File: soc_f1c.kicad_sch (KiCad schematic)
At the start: 30 parts, among them U3 F1C100S, Y1 24Mhz 12pF

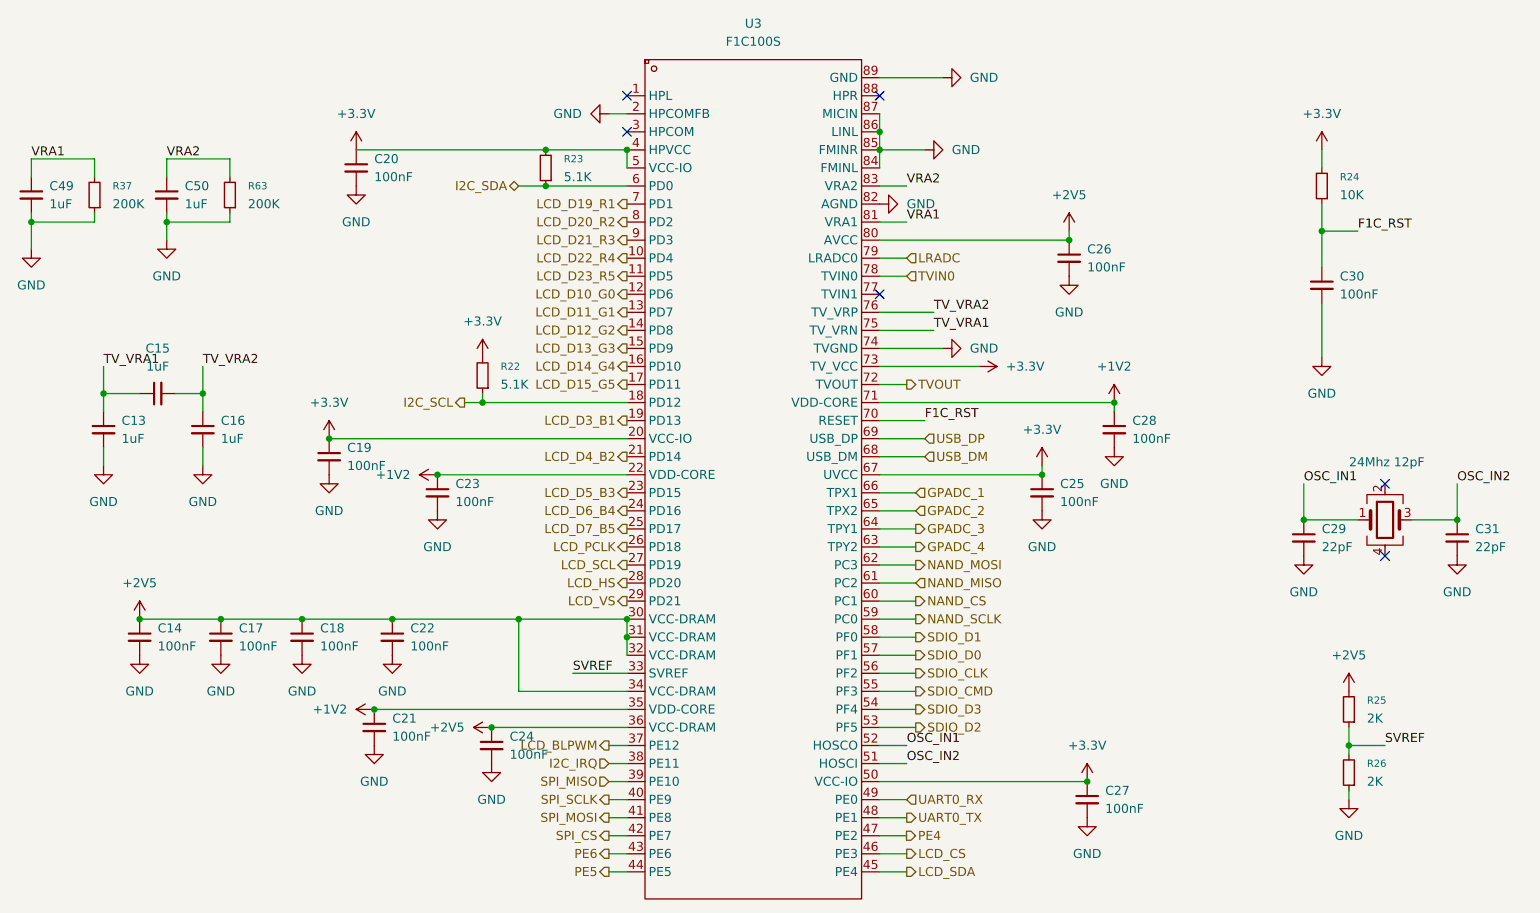
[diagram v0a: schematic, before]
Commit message: V0.3.1 bugfix
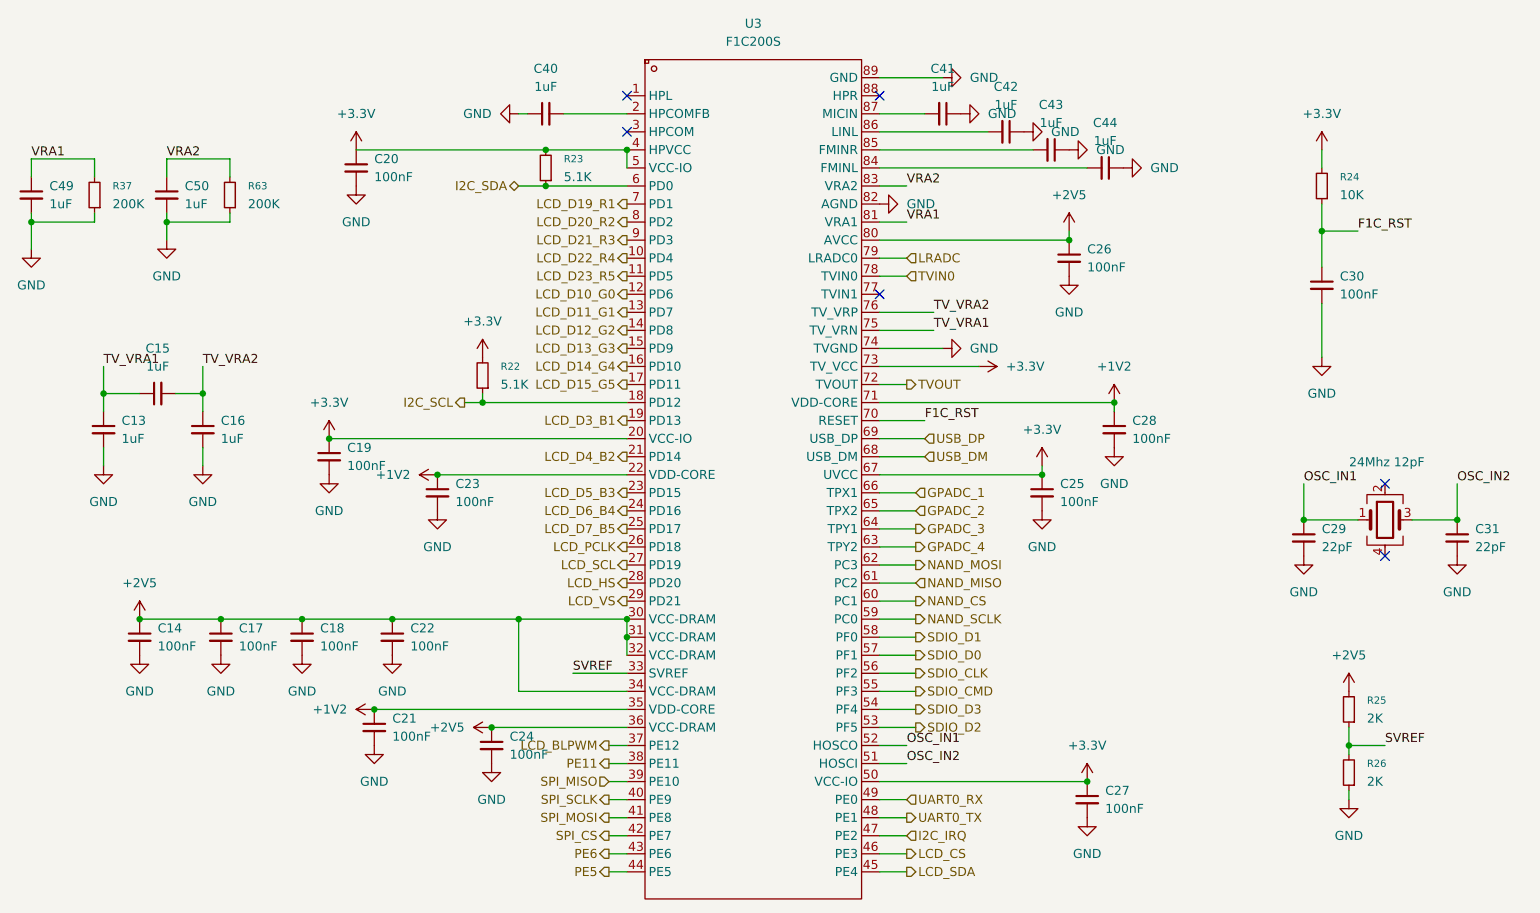
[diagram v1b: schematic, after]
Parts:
- added C40, C41, C42, C43, C44: 1uF, Capacitor_SMD:C_0603_1608Metric, symbol Device:C_Small
- U3: value F1C100S -> F1C200S; 特殊说明 (none) -> 不要购买”新版本“！
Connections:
- net PE4 is gone; now on net I2C_IRQ: U3.47 (PE2)
- net GND: now also C40.1, C41.1, C42.1, C43.1, C44.1; no longer U3.2 (HPCOMFB), U3.84 (FMINL), U3.85 (FMINR), U3.86 (LINL), U3.87 (MICIN)
- net I2C_IRQ: no longer U3.38 (PE11)
- new net: C43.2, U3.85 (FMINR)
- new net: C40.2, U3.2 (HPCOMFB)
- new net: C42.2, U3.86 (LINL)
- new net: C44.2, U3.84 (FMINL)
- new net: C41.2, U3.87 (MICIN)
- new net PE11: U3.38 (PE11)

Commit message: V0.5
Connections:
- net PE11 is gone; now on net LCD_CS: U3.38 (PE11)
- net LCD_CS: no longer U3.46 (PE3)
- net I2C_IRQ renamed PWR_SHUTDOWN
- new net PE3: U3.46 (PE3)
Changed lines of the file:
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@@
 		(comment 1 "V0.3 添加屏幕兼容接口，添加SD卡槽，优化布线")
 		(comment 2 "V0.3.1 BUG修复")
+		(comment 3 "土豆、星语Studio、爱莉希雅、所有复刻群友的支持！")
+		(comment 4 "V0.3.2 生产优化。特别感谢：（不分先后）和光、薄云、烟雨、WXNA、")
 	)
 	(junction
@@
 		)
 	)
-	(hierarchical_label "I2C_IRQ"
-		(shape input)
+	(hierarchical_label "PWR_SHUTDOWN"
+		(shape output)
 		(at 167.64 151.13 0)
 		(effects
@@
 		)
 	)
+	(hierarchical_label "LCD_CS"
+		(shape output)
+		(at 125.73 140.97 180)
+		(effects
+			(font
+				(size 1.27 1.27)
+			)
+			(justify right)
+		)
+	)
 	(hierarchical_label "LCD_D6_B4"
 		(shape output)
@@
 		)
 	)
-	(hierarchical_label "PE11"
-		(shape output)
-		(at 125.73 140.97 180)
-		(effects
-			(font
-				(size 1.27 1.27)
-			)
-			(justify right)
-		)
-	)
 	(hierarchical_label "SDIO_D1"
 		(shape output)
@@
 		)
 	)
-	(hierarchical_label "LCD_CS"
+	(hierarchical_label "SPI_CS"
+		(shape output)
+		(at 125.73 151.13 180)
+		(effects
+			(font
+				(size 1.27 1.27)
+			)
+			(justify right)
+		)
+	)
+	(hierarchical_label "LCD_SCL"
+		(shape output)
+		(at 128.27 113.03 180)
+		(effects
+			(font
+				(size 1.27 1.27)
+			)
+			(justify right)
+		)
+	)
+	(hierarchical_label "I2C_SCL"
+		(shape output)
+		(at 105.41 90.17 180)
+		(effects
+			(font
+				(size 1.27 1.27)
+			)
+			(justify right)
+		)
+	)
+	(hierarchical_label "SDIO_D2"
+		(shape output)
+		(at 168.91 135.89 0)
+		(effects
+			(font
+				(size 1.27 1.27)
+			)
+			(justify left)
+		)
+	)
+	(hierarchical_label "SDIO_CLK"
+		(shape output)
+		(at 168.91 128.27 0)
+		(effects
+			(font
+				(size 1.27 1.27)
+			)
+			(justify left)
+		)
+	)
+	(hierarchical_label "SPI_MOSI"
+		(shape output)
+		(at 125.73 148.59 180)
+		(effects
+			(font
+				(size 1.27 1.27)
+			)
+			(justify right)
+		)
+	)
+	(hierarchical_label "GPADC_3"
+		(shape output)
+		(at 168.91 107.95 0)
+		(effects
+			(font
+				(size 1.27 1.27)
+			)
+			(justify left)
+		)
+	)
+	(hierarchical_label "PE6"
+		(shape output)
+		(at 125.73 153.67 180)
+		(effects
+			(font
+				(size 1.27 1.27)
+			)
+			(justify right)
+		)
+	)
+	(hierarchical_label "LCD_PCLK"
+		(shape output)
+		(at 128.27 110.49 180)
+		(effects
+			(font
+				(size 1.27 1.27)
+			)
+			(justify right)
+		)
+	)
+	(hierarchical_label "SDIO_D3"
+		(shape output)
+		(at 168.91 133.35 0)
+		(effects
+			(font
+				(size 1.27 1.27)
+			)
+			(justify left)
+		)
+	)
+	(hierarchical_label "LCD_D10_G0"
+		(shape output)
+		(at 128.27 74.93 180)
+		(effects
+			(font
+				(size 1.27 1.27)
+			)
+			(justify right)
+		)
+	)
+	(hierarchical_label "SDIO_D0"
+		(shape output)
+		(at 168.91 125.73 0)
+		(effects
+			(font
+				(size 1.27 1.27)
+			)
+			(justify left)
+		)
+	)
+	(hierarchical_label "PE3"
 		(shape output)
 		(at 167.64 153.67 0)
 		(effects
 			(font
-				(size 1.27 1.27)
-			)
-			(justify left)
-		)
-	)
-	(hierarchical_label "SPI_CS"
-		(shape output)
-		(at 125.73 151.13 180)
-		(effects
-			(font
-				(size 1.27 1.27)
-			)
-			(justify right)
-		)
-	)
-	(hierarchical_label "LCD_SCL"
-		(shape output)
-		(at 128.27 113.03 180)
-		(effects
-			(font
-				(size 1.27 1.27)
-			)
-			(justify right)
-		)
-	)
-	(hierarchical_label "I2C_SCL"
-		(shape output)
-		(at 105.41 90.17 180)
-		(effects
-			(font
-				(size 1.27 1.27)
-			)
-			(justify right)
-		)
-	)
-	(hierarchical_label "SDIO_D2"
-		(shape output)
-		(at 168.91 135.89 0)
-		(effects
-			(font
-				(size 1.27 1.27)
-			)
-			(justify left)
-		)
-	)
-	(hierarchical_label "SDIO_CLK"
-		(shape output)
-		(at 168.91 128.27 0)
-		(effects
-			(font
-				(size 1.27 1.27)
-			)
-			(justify left)
-		)
-	)
-	(hierarchical_label "SPI_MOSI"
-		(shape output)
-		(at 125.73 148.59 180)
-		(effects
-			(font
-				(size 1.27 1.27)
-			)
-			(justify right)
-		)
-	)
-	(hierarchical_label "GPADC_3"
-		(shape output)
-		(at 168.91 107.95 0)
-		(effects
-			(font
-				(size 1.27 1.27)
-			)
-			(justify left)
-		)
-	)
-	(hierarchical_label "PE6"
-		(shape output)
-		(at 125.73 153.67 180)
-		(effects
-			(font
-				(size 1.27 1.27)
-			)
-			(justify right)
-		)
-	)
-	(hierarchical_label "LCD_PCLK"
-		(shape output)
-		(at 128.27 110.49 180)
-		(effects
-			(font
-				(size 1.27 1.27)
-			)
-			(justify right)
-		)
-	)
-	(hierarchical_label "SDIO_D3"
-		(shape output)
-		(at 168.91 133.35 0)
-		(effects
-			(font
-				(size 1.27 1.27)
-			)
-			(justify left)
-		)
-	)
-	(hierarchical_label "LCD_D10_G0"
-		(shape output)
-		(at 128.27 74.93 180)
-		(effects
-			(font
-				(size 1.27 1.27)
-			)
-			(justify right)
-		)
-	)
-	(hierarchical_label "SDIO_D0"
-		(shape output)
-		(at 168.91 125.73 0)
-		(effects
-			(font
